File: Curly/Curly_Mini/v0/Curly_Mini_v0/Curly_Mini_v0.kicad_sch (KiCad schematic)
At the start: 3 parts, among them J1 DEBUG_PORT, U1 RP2040, U2 MCP25625T-E_ML

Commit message: Curly partially done
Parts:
- added C1, C2, C6: 100n, Capacitor_SMD:C_0402_1005Metric, symbol Device:C_Small
- added C3, C4, C5: 2u2, Capacitor_SMD:C_0402_1005Metric, symbol Device:C_Small
- added C7, C8: 33p C0G, Capacitor_SMD:C_0402_1005Metric, symbol Device:C_Small
- added FB1: FB_0603, Capacitor_SMD:C_0402_1005Metric, symbol Device:FerriteBead_Small
- added R1: 4k7, Resistor_SMD:R_0402_1005Metric, symbol Device:R_Small_US
- added R2: 1k 1%, Resistor_SMD:R_0402_1005Metric, symbol Device:R_Small_US
- added R3, R4: 27R, Resistor_SMD:R_0402_1005Metric, symbol Device:R_Small_US
- added U4: W25Q16JVUXIQ_TR, ICDB_Curly:IC_W25Q16JVUXIQ_TR, symbol ICDB_Curly:W25Q16JVUXIQ_TR
- added Y2: 12.000 MHz, C9002, Crystal:Crystal_SMD_3225-4Pin_3.2x2.5mm, symbol Device:Crystal_GND24
- U2: footprint MCP25625T-E_ML:QFN65P600X600X100-29N -> ICDB_Curly:QFN65P600X600X100-29N
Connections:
- net GND: now also C1.2, C2.2, C3.2, C4.2, C5.2, C6.2, C7.2, C8.2, U4.4 (GND), U4.9 (EXP), Y2.2, Y2.4
- net +3V3: now reaches U1.1 (IOVDD), U1.10 (IOVDD), U1.22 (IOVDD), U1.33 (IOVDD), U1.42 (IOVDD), U1.49 (IOVDD)
- net +3V3: now also U1.44 (VREG_IN), U1.48 (USB_VDD), C1.1, C5.1, C6.1, FB1.1, R1.1, U4.8 (VCC)
- net SPI1_SCK: now reaches U1.13 (GPIO10)
- net SPI1_SCK: now also U2.26 (SCK)
- net SPI1_TX: now reaches U1.14 (GPIO11)
- net SPI1_TX: now also U2.27 (SI)
- net SPI1_RX: now reaches U1.15 (GPIO12)
- net SPI1_RX: now also U2.28 (SO)
- net SPI1_CSn: now reaches U1.16 (GPIO13)
- net SPI1_CSn: now also U2.1 (~{CS})
- net XIN: now reaches U1.20 (XIN)
- net XIN: now also C8.1, Y2.1
- net at U1.21 (XOUT): now also R2.2
- net +1V1: now reaches U1.23 (DVDD), U1.50 (DVDD)
- net +1V1: now also U1.45 (VREG_VOUT), C2.1, C3.1
- net ~{EXT_RESET}: now reaches U1.26 (RUN)
- net ~{EXT_RESET}: now also R1.2
- net VDDA: now reaches U1.43 (ADC_AVDD)
- net VDDA: now also C4.1, FB1.2
- net at U1.46 (USB_DM): now also R4.2
- net at U1.47 (USB_DP): now also R3.2
- net QSPI_SD3: now reaches U1.51 (QSPI_SD3)
- net QSPI_SD3: now also U4.7 (~{HOLD}/~{RESET}/IO3)
- net QSPI_SCLK: now reaches U1.52 (QSPI_SCLK)
- net QSPI_SCLK: now also U4.6 (CLK)
- net QSPI_SD0: now reaches U1.53 (QSPI_SD0)
- net QSPI_SD0: now also U4.5 (DI/IO0)
- net QSPI_SD2: now reaches U1.54 (QSPI_SD2)
- net QSPI_SD2: now also U4.3 (~{WP}/IO2)
- net QSPI_SD1: now reaches U1.55 (QSPI_SD1)
- net QSPI_SD1: now also U4.2 (DO/IO1)
- net ~{QSPI_CSN}: now reaches U1.56 (QSPI_SS)
- net ~{QSPI_CSN}: now also U4.1 (~{CS})
- net CAN_TXVR_STBY: now reaches U2.15 (STBY)
- new net USB_DM: R4.1
- new net USB_DP: R3.1
- new net XOUT: C7.1, R2.1, Y2.3
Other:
- note added: "20pF Crystal, 80R ESR 33p / 2 == 16.5p Allowance for 3.5p wiring and lead capacitance"
- note added: "LCSC/JLC PART NUMBERS (BASIC/EXTENDED) 100n 0402 -> C307331 (B) 2u2 0402 -> C12530 (B) 12MHz XTAL -> C9002 (B) 33pF C0G 0402 -> C1562 (B) 1kR 0402 -> C11702 (B)"

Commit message: Curly Mini almost done :)
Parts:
- added C10, C12, C14, C16, C17, C18, C21, C23, C24, C25, C26, C27: 100n, Capacitor_SMD:C_0402_1005Metric, symbol Device:C_Small
- added C11, C13, C15, C19, C28, C29, C9: 2u2, Capacitor_SMD:C_0402_1005Metric, symbol Device:C_Small
- added C20, C22: 10u, Capacitor_SMD:C_0603_1608Metric, symbol Device:C_Small
- added J2, J3: Conn_01x01_Pin, ICDB_Waffle:ICDB_Castellated_Pad, symbol Connector:Conn_01x01_Pin
- added U3: XC6206PxxxMR, Package_TO_SOT_SMD:SOT-23-3, symbol Regulator_Linear:XC6206PxxxMR
- added U5: SE8650X2-HF, Package_TO_SOT_SMD:SOT-23-3, symbol Regulator_Linear:XC6206PxxxMR
- FB1: footprint Capacitor_SMD:C_0402_1005Metric -> Inductor_SMD:L_0603_1608Metric
- J1: footprint (none) -> Connector_JST:JST_SH_BM03B-SRSS-TB_1x03-1MP_P1.00mm_Vertical
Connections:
- net +1V1: now also C10.1, C11.1, C12.1, C9.1
- net +3V3: now also U2.11 (VIO), U2.3 (VDD), C13.1, C14.1, C15.1, C16.1, C17.1, C18.1, C19.1, C20.1, C21.1, C26.1, C27.1, C28.1, U3.2 (VO)
- net GND: now also U2.18 (VSS), U2.22 (GND), U2.29 (EP), C10.2, C11.2, C12.2, C13.2, C14.2, C15.2, C16.2, C17.2, C18.2, C19.2, C20.2, C21.2, C22.2, C23.2, C24.2, C25.2, C26.2, C27.2, C28.2, C29.2, C9.2, U3.1 (GND), U5.1 (GND)
- net SPI1_SCK: now also U1.17 (GPIO14); no longer U1.13 (GPIO10)
- net SPI1_TX: now also U1.18 (GPIO15); no longer U1.14 (GPIO11)
- net at U2.10 (RXD): now also U2.5 (RXCAN)
- net CANL: now reaches U2.12 (CANL)
- net CANL: now also J2.1 (Pin_1)
- net CANH: now reaches U2.13 (CANH)
- net CANH: now also J3.1 (Pin_1)
- net at U2.16 (TXD): now also U2.4 (TXCAN)
- net +5V: now reaches U2.19 (VDDA)
- net +5V: now also C22.1, C23.1, C25.1, C29.1, U3.3 (VI), U5.2 (VO)
- net ~{CAN_RX_BUF1}: now reaches U2.23 (~{RX1BF})
- net ~{CAN_RX_BUF0}: now reaches U2.24 (~{RX0BF})
- net ~{CAN_RX_INT}: now reaches U2.25 (~{INT})
- new net VDC: C24.1, U5.3 (VI)
- no-connect marks 0 -> 1
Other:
- note added: "6V - 80V in MAX 7V - 60V Recommended Limits Specified Operating Range: 7V - 48V 200mA"
- note added: "LCSC/JLC PART NUMBERS (BASIC/EXTENDED) 100n 0402 -> C307331 (B) 2u2 0402 -> C12530 (B) 10u 0603 -> C96446 (B) 12MHz XTAL -> C9002 (B) 33pF C0G 0402 -> C1562 (B) 1kR 0402 -> C11702 (B) Ferrite 0603 -> C1002 (B) 3V3 LDO SOT23-3 -> C5446 (B) 5V LDO SOT23-3 -> C496615 (E)"
- note added: "Must be 50V rated cap!!"
- note added: "SPI1 Peripheral tied to CAN interface"
- note added: "Torex, C5446"
- note removed: "LCSC/JLC PART NUMBERS (BASIC/EXTENDED) 100n 0402 -> C307331 (B) 2u2 0402 -> C12530 (B) 12MHz XTAL -> C9002 (B) 33pF C0G 0402 -> C1562 (B) 1kR 0402 -> C11702 (B)"
- moved on the sheet: R1, U2

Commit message: Curly Mini almost done (again) :)
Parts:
- removed C12: 100n, Capacitor_SMD:C_0402_1005Metric, symbol Device:C_Small
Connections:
- net CAN_TXVR_STBY: now also U1.31 (GPIO20)
- net ~{CAN_RX_BUF0}: now also U1.28 (GPIO17)
- net ~{CAN_RX_BUF1}: now also U1.29 (GPIO18)
- net ~{CAN_RX_INT}: now also U1.27 (GPIO16)
- net ~{CAN_TX2_RTS}: now reaches U1.11 (GPIO8)
- net ~{CAN_TX2_RTS}: now also U2.9 (~{TX2RTS})
- net ~{CAN_TX1_RTS}: now reaches U1.12 (GPIO9)
- net ~{CAN_TX1_RTS}: now also U2.8 (~{TX1RTS})
- net ~{CAN_TX0_RTS}: now reaches U1.13 (GPIO10)
- net ~{CAN_TX0_RTS}: now also U2.7 (~{TX0RTS})
- net ~{CAN_RESET}: now reaches U1.14 (GPIO11)
- net ~{CAN_RESET}: now also U2.2 (~{RESET})
- net MCP25625_CLK: now reaches U1.30 (GPIO19)
- net MCP25625_CLK: now also U2.21 (OSC1)
- no-connect marks 1 -> 2
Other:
- note added: "Can be used to queue messages and send on RQ"
- moved on the sheet: C25, C26, C27, C28, C29, U2

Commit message: Curly Mini RS232 completed
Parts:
- added C12, C30, C31, C32, C33: 100n, Capacitor_SMD:C_0402_1005Metric, symbol Device:C_Small
- added C34: 2u2, Capacitor_SMD:C_0402_1005Metric, symbol Device:C_Small
- added J4, J5, J6, J7: Conn_01x01_Pin, ICDB_Waffle:ICDB_Castellated_Pad, symbol Connector:Conn_01x01_Pin
- added U6: MAX3232, Package_SO:TSSOP-16_4.4x5mm_P0.65mm, symbol Interface_UART:MAX3232
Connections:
- net +3V3: now also C33.1, C34.1, U6.16 (VCC)
- net GND: now also C31.2, C32.2, C33.2, C34.2, U6.15 (GND)
- net UART_0_TX: now reaches U1.2 (GPIO0)
- net UART_0_TX: now also U6.11 (T1IN)
- net UART_0_RX: now reaches U1.3 (GPIO1)
- net UART_0_RX: now also U6.12 (R1OUT)
- net UART_1_TX: now reaches U1.6 (GPIO4)
- net UART_1_TX: now also U6.10 (T2IN)
- net UART_1_RX: now reaches U1.7 (GPIO5)
- net UART_1_RX: now also U6.9 (R2OUT)
- new net: C32.1, U6.2 (VS+)
- new net: C30.1, U6.1 (C1+)
- new net: C30.2, U6.3 (C1-)
- new net: C12.1, U6.4 (C2+)
- new net: C12.2, U6.5 (C2-)
- new net: C31.1, U6.6 (VS-)
- new net RS232_0_RX: J7.1 (Pin_1), U6.13 (R1IN)
- new net RS232_0_TX: J6.1 (Pin_1), U6.14 (T1OUT)
- new net RS232_1_RX: J5.1 (Pin_1), U6.8 (R2IN)
- new net RS232_1_TX: J4.1 (Pin_1), U6.7 (T2OUT)
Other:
- note added: "LCSC/JLC PART NUMBERS (BASIC/EXTENDED) 100n 0402 -> C307331 (B) 2u2 0402 -> C12530 (B) 10u 0603 -> C96446 (B) 12MHz XTAL -> C9002 (B) 33pF C0G 0402 -> C1562 (B) 1kR 0402 -> C11702 (B) Ferrite 0603 -> C1002 (B) 3V3 LDO SOT23-3 -> C5446 (B) 5V LDO SOT23-3 -> C496615 (E) MAX3232 TSSOP16 -> C11317 (E)"
- note removed: "LCSC/JLC PART NUMBERS (BASIC/EXTENDED) 100n 0402 -> C307331 (B) 2u2 0402 -> C12530 (B) 10u 0603 -> C96446 (B) 12MHz XTAL -> C9002 (B) 33pF C0G 0402 -> C1562 (B) 1kR 0402 -> C11702 (B) Ferrite 0603 -> C1002 (B) 3V3 LDO SOT23-3 -> C5446 (B) 5V LDO SOT23-3 -> C496615 (E)"
- moved on the sheet: C1, C20, C21, C22, C23, C24, U3, U4, U5

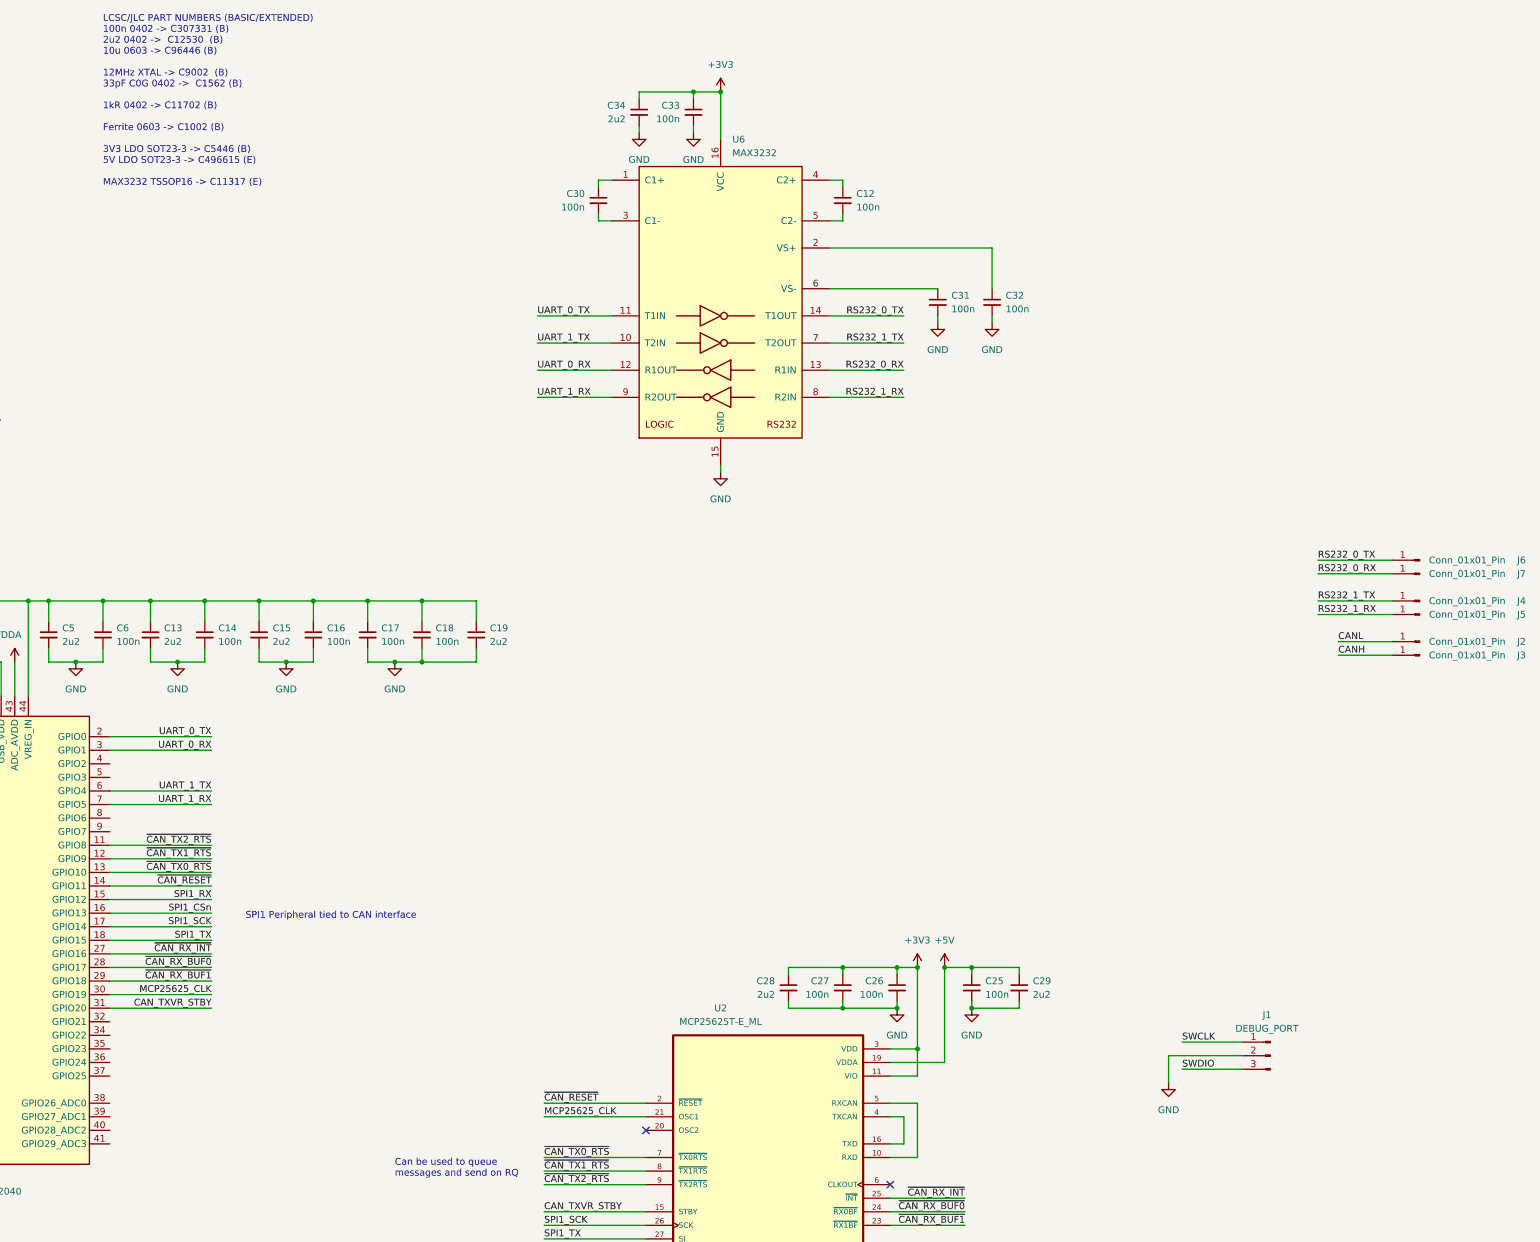
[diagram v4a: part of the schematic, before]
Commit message: Curly Mini Prelim layout done
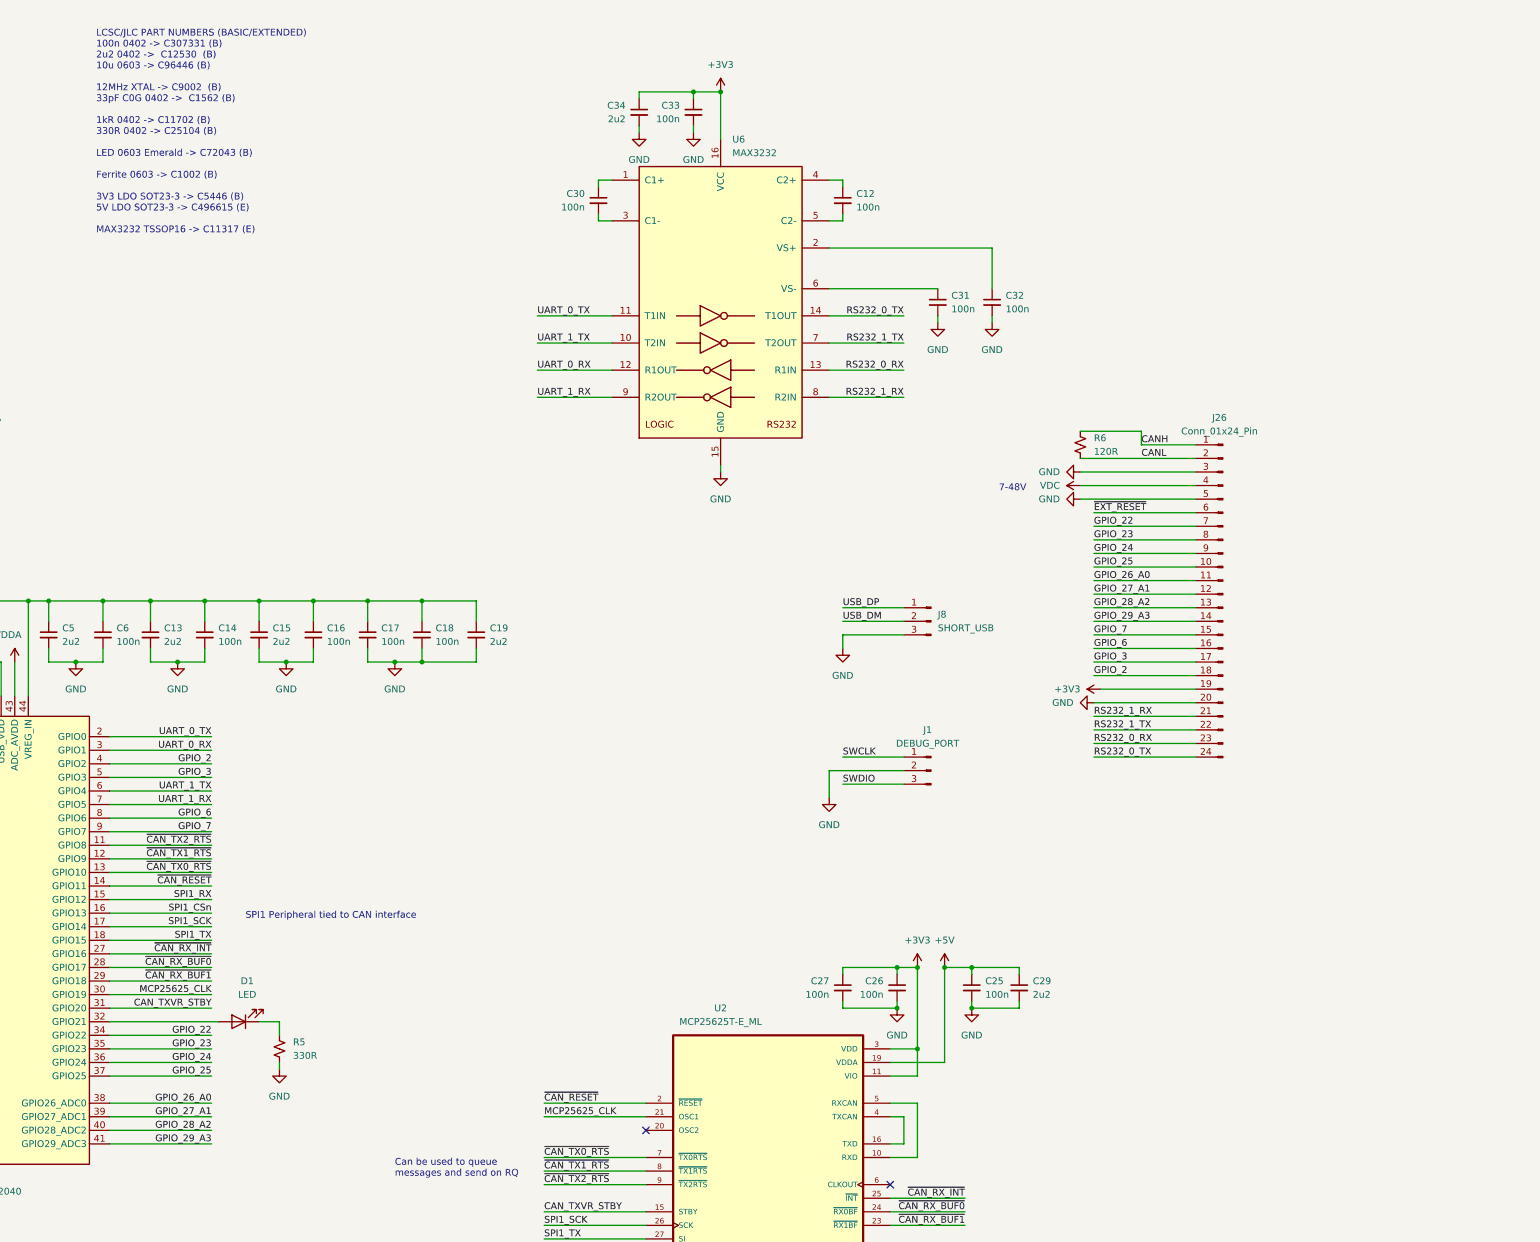
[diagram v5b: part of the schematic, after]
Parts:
- removed C28: 2u2, Capacitor_SMD:C_0402_1005Metric, symbol Device:C_Small
- removed J2, J3, J4, J5, J6, J7: Conn_01x01_Pin, ICDB_Waffle:ICDB_Castellated_Pad, symbol Connector:Conn_01x01_Pin
- added D1: LED, LED_SMD:LED_0603_1608Metric, symbol Device:LED
- added J26: Conn_01x24_Pin, ICDB_Curly:ICDB_Curly_Edge_Conn, symbol Connector:Conn_01x24_Pin
- added J8: SHORT_USB, Connector_PinSocket_2.54mm:PinSocket_1x03_P2.54mm_Vertical, symbol Connector:Conn_01x03_Pin
- added R5: 330R, Resistor_SMD:R_0402_1005Metric, symbol Device:R_Small_US
- added R6: 120R, Resistor_SMD:R_0805_2012Metric_Pad1.20x1.40mm_HandSolder, symbol Device:R_Small_US
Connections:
- net +3V3: now also J26.19 (Pin_19)
- net CANH: now also J26.1 (Pin_1), R6.1
- net CANL: now also J26.2 (Pin_2), R6.2
- net GND: now also J26.20 (Pin_20), J26.3 (Pin_3), J26.5 (Pin_5), J8.3 (Pin_3), R5.2
- net RS232_0_RX: now also J26.23 (Pin_23)
- net RS232_0_TX: now also J26.24 (Pin_24)
- net RS232_1_RX: now also J26.21 (Pin_21)
- net RS232_1_TX: now also J26.22 (Pin_22)
- net USB_DM: now also J8.2 (Pin_2)
- net USB_DP: now also J8.1 (Pin_1)
- net VDC: now also J26.4 (Pin_4)
- net ~{EXT_RESET}: now also J26.6 (Pin_6)
- net at U1.32 (GPIO21): now also D1.2 (A)
- net GPIO_22: now reaches U1.34 (GPIO22)
- net GPIO_22: now also J26.7 (Pin_7)
- net GPIO_23: now reaches U1.35 (GPIO23)
- net GPIO_23: now also J26.8 (Pin_8)
- net GPIO_24: now reaches U1.36 (GPIO24)
- net GPIO_24: now also J26.9 (Pin_9)
- net GPIO_25: now reaches U1.37 (GPIO25)
- net GPIO_25: now also J26.10 (Pin_10)
- net GPIO_26_A0: now reaches U1.38 (GPIO26_ADC0)
- net GPIO_26_A0: now also J26.11 (Pin_11)
- net GPIO_27_A1: now reaches U1.39 (GPIO27_ADC1)
- net GPIO_27_A1: now also J26.12 (Pin_12)
- net GPIO_2: now reaches U1.4 (GPIO2)
- net GPIO_2: now also J26.18 (Pin_18)
- net GPIO_28_A2: now reaches U1.40 (GPIO28_ADC2)
- net GPIO_28_A2: now also J26.13 (Pin_13)
- net GPIO_29_A3: now reaches U1.41 (GPIO29_ADC3)
- net GPIO_29_A3: now also J26.14 (Pin_14)
- net GPIO_3: now reaches U1.5 (GPIO3)
- net GPIO_3: now also J26.17 (Pin_17)
- net GPIO_6: now reaches U1.8 (GPIO6)
- net GPIO_6: now also J26.16 (Pin_16)
- net GPIO_7: now reaches U1.9 (GPIO7)
- net GPIO_7: now also J26.15 (Pin_15)
- new net: D1.1 (K), R5.1
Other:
- note added: "7-48V"
- note added: "LCSC/JLC PART NUMBERS (BASIC/EXTENDED) 100n 0402 -> C307331 (B) 2u2 0402 -> C12530 (B) 10u 0603 -> C96446 (B) 12MHz XTAL -> C9002 (B) 33pF C0G 0402 -> C1562 (B) 1kR 0402 -> C11702 (B) 330R 0402 -> C25104 (B) LED 0603 Emerald -> C72043 (B) Ferrite 0603 -> C1002 (B) 3V3 LDO SOT23-3 -> C5446 (B) 5V LDO SOT23-3 -> C496615 (E) MAX3232 TSSOP16 -> C11317 (E)"
- note removed: "LCSC/JLC PART NUMBERS (BASIC/EXTENDED) 100n 0402 -> C307331 (B) 2u2 0402 -> C12530 (B) 10u 0603 -> C96446 (B) 12MHz XTAL -> C9002 (B) 33pF C0G 0402 -> C1562 (B) 1kR 0402 -> C11702 (B) Ferrite 0603 -> C1002 (B) 3V3 LDO SOT23-3 -> C5446 (B) 5V LDO SOT23-3 -> C496615 (E) MAX3232 TSSOP16 -> C11317 (E)"
- moved on the sheet: J1

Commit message: Final v0 revision made, JLC fab files provided. Castellated holes are ultra expensive, moved to 2 sided edge connect
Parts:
- R1: value 4k7 -> 5k1
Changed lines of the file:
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@@
       (effects (font (size 1.27 1.27)) (justify left))
     )
-    (property "Value" "4k7" (at 36.83 140.97 0)
+    (property "Value" "5k1" (at 36.83 140.97 0)
       (effects (font (size 1.27 1.27)) (justify left))
     )

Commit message: Added USB ESD Protection, USB Boot button - Curly
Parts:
- added D2, D3: ACPDQC3V3T-HF, ICDB_Curly:0402C-SOD-923F, symbol Device:D_TVS
- added R7: 10k, Resistor_SMD:R_0402_1005Metric, symbol Device:R_Small_US
- added SW1: SW_SPST, ICDB_Curly:TPS850 J14Q V SMTR LFS, symbol Switch:SW_SPST
- added TP1: TestPoint, TestPoint:TestPoint_Pad_D2.0mm, symbol Connector:TestPoint
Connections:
- net GND: now also D2.1 (A1), D3.1 (A1), R7.2, TP1.1
- net USB_DM: now also D2.2 (A2)
- net USB_DP: now also D3.2 (A2)
- net ~{QSPI_CSN}: now also SW1.1 (A)
- new net: R7.1, SW1.2 (B)
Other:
- note added: "LCSC: C2443351"
- note added: "LCSC: C2759976"
